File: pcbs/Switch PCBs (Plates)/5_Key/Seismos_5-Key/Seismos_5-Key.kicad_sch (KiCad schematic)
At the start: 11 parts, among them J1 SM10B-SRSS-TB_(LF)(SN), SW1 Switch_SK6812-E_Diode, SW2 Switch_SK6812-E_Diode, SW3 Switch_SK6812-E_Diode, SW4 Switch_SK6812-E_Diode, SW5 Switch_SK6812-E_Diode

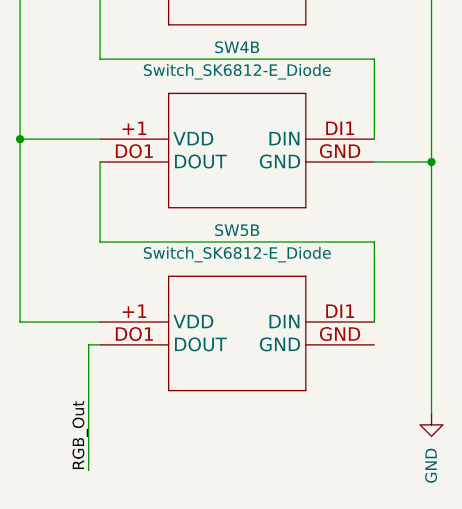
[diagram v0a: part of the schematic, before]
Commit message: Release v1.1
***NOTE***: If you have a previous commit, please update your files.
This commit fixes the incorrect RGB pinout and power switch as the
RGB footprint was incorrect.
The power switch behaviour is also fixed in this commit so the position
matches on both sides.
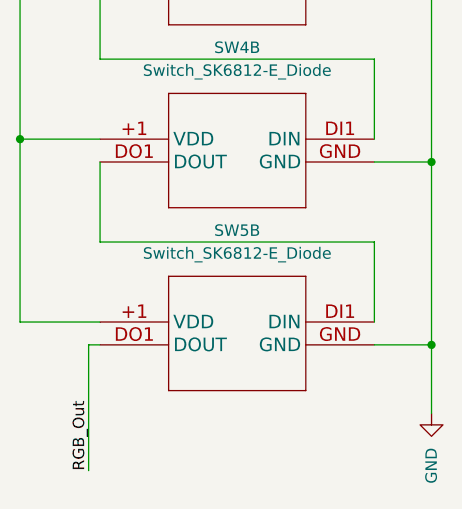
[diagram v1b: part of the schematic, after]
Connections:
- net GND: now also SW5.GND
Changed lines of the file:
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@@
   (junction (at 232.41 67.31) (diameter 0) (color 0 0 0 0)
+  )
+  (junction (at 232.41 128.27) (diameter 0) (color 0 0 0 0)
   )
   (junction (at 232.41 107.95) (diameter 0) (color 0 0 0 0)
@@
     (stroke (width 0) (type default))
   )
+  (wire (pts (xy 232.41 128.27) (xy 232.41 135.89))
+    (stroke (width 0) (type default))
+  )
   (wire (pts (xy 195.58 55.88) (xy 226.06 55.88))
     (stroke (width 0) (type default))
@@
     (stroke (width 0) (type default))
   )
+  (wire (pts (xy 226.06 128.27) (xy 232.41 128.27))
+    (stroke (width 0) (type default))
+  )
   (wire (pts (xy 125.73 101.6) (xy 135.89 101.6))
     (stroke (width 0) (type default))
@@
     (stroke (width 0) (type default))
   )
-  (wire (pts (xy 232.41 107.95) (xy 232.41 135.89))
+  (wire (pts (xy 232.41 107.95) (xy 232.41 128.27))
     (stroke (width 0) (type default))
   )
